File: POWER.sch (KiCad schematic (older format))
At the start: 59 parts, among them Q201 PZTA42, Q202 PZTA42, Q203 BCP51, U201 MAX1555, U202 BQ24400, U203 TPS61021A

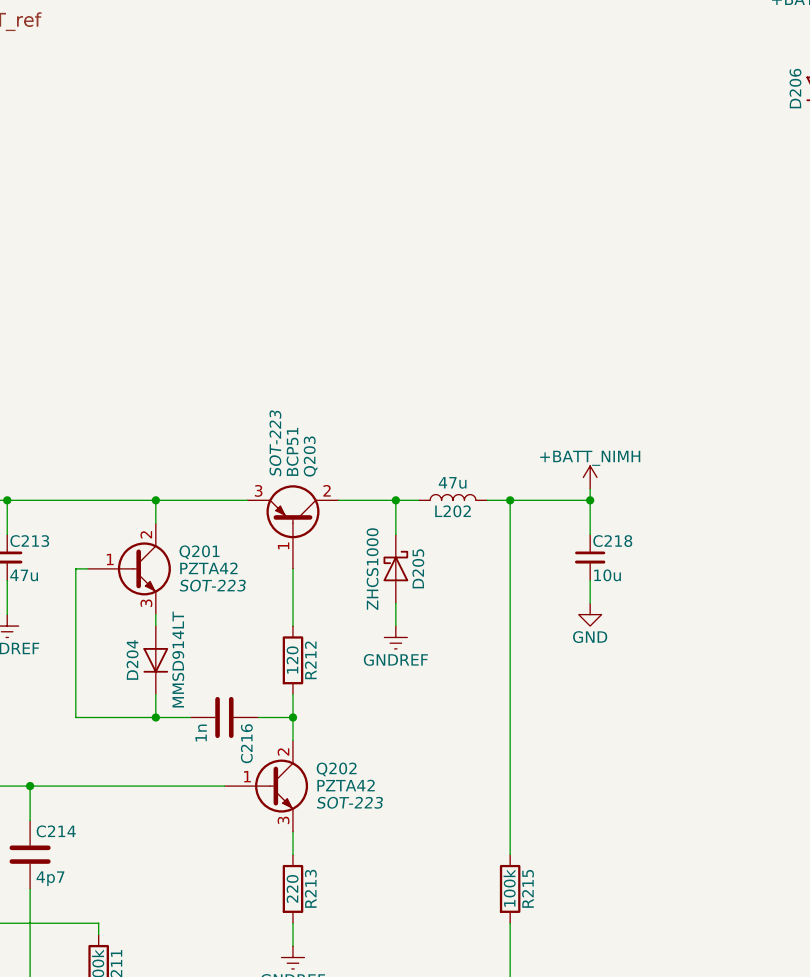
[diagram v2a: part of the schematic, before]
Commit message: Created netlist with current components Foreward Annotation to Board
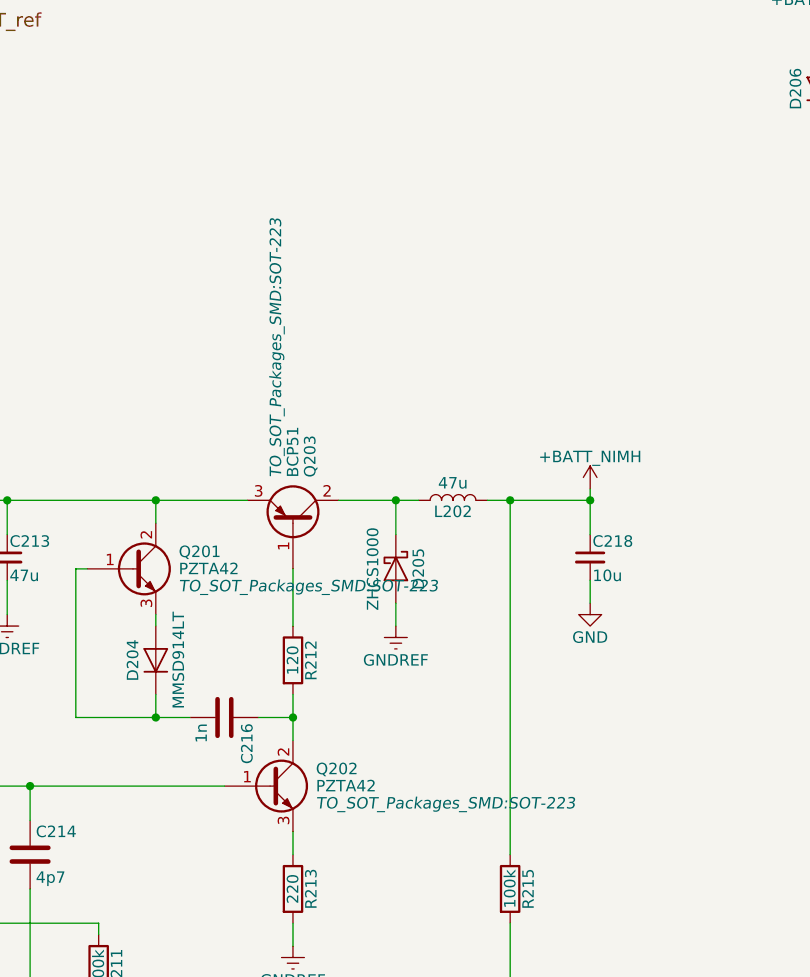
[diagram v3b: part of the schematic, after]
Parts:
- C204, C205, C206, C207, C208, C209, C210, C215, C219: footprint Capacitors_SMD:C_0603 -> Capacitors_SMD:C_0402
- C211: footprint (none) -> Capacitors_SMD:C_0603
- C212, C214, C216, C217: footprint (none) -> Capacitors_SMD:C_0402
- C213: footprint Capacitors_SMD:C_0603 -> Capacitors_SMD:C_0805
- D201, D202, D203, D204, D205, D206, D207: footprint (none) -> Diodes_SMD:DD-PAK_TO263_SingleDiode
- L201: footprint Resistors_SMD:R_0603 -> Choke_SMD:Choke_SMD_1206_Standard
- L202: footprint (none) -> Choke_SMD:Choke_SMD_1206_Standard
- Q201, Q202, Q203: footprint SOT-223 -> TO_SOT_Packages_SMD:SOT-223
- R201, R202, R203, R204, R205, R207, R208, R211, R217, R218: footprint Resistors_SMD:R_0603 -> Resistors_SMD:R_0402
- R206, R209, R210, R212, R213, R214, R215, R216: footprint (none) -> Resistors_SMD:R_0402
- TP201, TP202, TP203, TP204, TP205, TP206: footprint buttons:TP -> NokiaRetroFit:TP
- U202: footprint (none) -> SMD_Packages:SOIC-8-N

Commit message: Modification for STM32 adaption
For the Hackaday Prize 2017 I decided to switch to STM32 as CPU

*Power system was modified to just contain the charge IC,
*Boost converter for high voltage peripherals
*Buck converter for 3V3 for CPU and switchable NVCC_3V3
   for peripherie

CPU signals are routed and pinmux is done in firmware folder.

SD-Card has 4bit Interface

WiFi module ESP8266 is connected via UART

Wolfson Ausio codec is connected via SAI

Two digital microphones for noise canceling

Rumble Motor driver

LCD is connected via it's own I2C interface
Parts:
- removed C201, C218: 10u, Capacitors_SMD:C_0603, symbol C_Small
- removed C205: 100n, Capacitors_SMD:C_0402, symbol C_Small
- removed C208: 1n, Capacitors_SMD:C_0402, symbol C_Small
- removed C211: 330n, Capacitors_SMD:C_0603, symbol C
- removed C212: 2n2, Capacitors_SMD:C_0402, symbol C
- removed C213: 47u, Capacitors_SMD:C_0805, symbol C_Small
- removed C214: 4p7, Capacitors_SMD:C_0402, symbol C
- removed C216: 1n, Capacitors_SMD:C_0402, symbol C
- removed C217: 100n, Capacitors_SMD:C_0402, symbol C
- removed D201: BZT52-C5V1, Diodes_SMD:DD-PAK_TO263_SingleDiode, symbol D
- removed D202, D204, D206, D207: MMSD914LT, Diodes_SMD:DD-PAK_TO263_SingleDiode, symbol D
- removed D203: S1A, Diodes_SMD:DD-PAK_TO263_SingleDiode, symbol D
- removed D205: ZHCS1000, Diodes_SMD:DD-PAK_TO263_SingleDiode, symbol D_Schottky
- removed L202: 47u, Choke_SMD:Choke_SMD_1206_Standard, symbol L
- removed Q201, Q202: PZTA42, TO_SOT_Packages_SMD:SOT-223, symbol PZTA42
- removed Q203: BCP51, TO_SOT_Packages_SMD:SOT-223, symbol BCP51
- removed R216: 1M, Resistors_SMD:R_0402, symbol R
- removed U202: BQ24400, SMD_Packages:SOIC-8-N, symbol BQ24400
- added L202: 2u2, Choke_SMD:Choke_SMD_1206_Standard, symbol L_Small
- added U202: TPS62742, symbol TPS62742
- C204, C206, C207, C209, C210, C215, C219: footprint Capacitors_SMD:C_0402 -> Capacitors_SMD:C_0402_NoSilk
- C220: footprint Capacitors_SMD:C_0603 -> Capacitors_SMD:C_0402_NoSilk
- R201, R202, R203, R204, R207, R208, R217, R218: footprint Resistors_SMD:R_0402 -> Resistors_SMD:R_0402_NoSilk
- R205: value 1k -> 0; footprint Resistors_SMD:R_0402 -> Resistors_SMD:R_0402_NoSilk
- R206: value 6k81 -> 0; footprint Resistors_SMD:R_0402 -> Resistors_SMD:R_0402_NoSilk
- R209: value 0R05 -> 0; footprint Resistors_SMD:R_0402 -> Resistors_SMD:R_0402_NoSilk
- R210: value 1k1 -> 0; footprint Resistors_SMD:R_0402 -> Resistors_SMD:R_0402_NoSilk
- R211, R214: value 100k -> 0; footprint Resistors_SMD:R_0402 -> Resistors_SMD:R_0402_NoSilk
- R212: value 120 -> 0; footprint Resistors_SMD:R_0402 -> Resistors_SMD:R_0402_NoSilk
- R213: value 220 -> 0; footprint Resistors_SMD:R_0402 -> Resistors_SMD:R_0402_NoSilk
- R215: value 100k -> 10k; footprint Resistors_SMD:R_0402 -> Resistors_SMD:R_0402_NoSilk
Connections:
- net +BATT_LIPO: now also R205.2, R206.2, R209.2, R210.2, U202.1 (VIN), U202.12 (EN); no longer R215.1
- net GND: now also R211.1, R212.1, R213.1, R214.1, U202.13 (TP), U202.3 (GND); no longer R206.2, R209.2
- net GNDREF: no longer R209.1, R210.2, R213.2
- net ~CHARGING: no longer R211.2
- net at R210.1: now also R214.2, U202.8 (VSEL4)
- net at R206.1: now also R212.2, U202.10 (VSEL2)
- net 3V3_PG: now reaches R215.2
- net 3V3_PG: now also U202.7 (PG); no longer R214.1
- net at R205.1: now also R211.2, U202.11 (VSEL1)
- new net: L202.1, U202.2 (SW)
- new net: R209.1, R213.2, U202.9 (VSEL3)
- new net 3V3: L202.2, R215.1, U202.5 (VOUT)
- new net NVCC_3V3: U202.6 (LOAD)
- new net NVCC_3V3_EN: U202.4 (CTRL)
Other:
- note added: "LiPo min 3.7V"
- note added: "Switched Rail"
- note removed: "+15V"
- note removed: "+3.3VDAC"
- note removed: "+BATT_LIPO"
- note removed: "+BATT_NIMH"
- note removed: "-"
- note removed: "0.675V"
- note removed: "1.1V"
- note removed: "1.25A"
- note removed: "1.35V"
- note removed: "1.5A"
- note removed: "1.5V"
- note removed: "1.75A"
- note removed: "1.8V"
- note removed: "1.8V .. 3V"
- note removed: "100mA"
- note removed: "1A"
- note removed: "1V"
- note removed: "1mA"
- note removed: "2.4V"
- note removed: "2.4V NiMH option"
- note removed: "2.85V .. 3.3V"
- note removed: "2.8V"
- note removed: "250mA"
- note removed: "3,5A"
- note removed: "3.3V"
- note removed: "3.7V"
- note removed: "350mA"
- note removed: "4V"
- note removed: "4V_BST"
- note removed: "50mV max\n-50mV min"
- note removed: "5A"
- note removed: "5V"
- note removed: "5V_VBUS"
- note removed: "600mA"
- note removed: "?"
- note removed: "Battery"
- note removed: "Comment"
- note removed: "Current (max)"
- note removed: "DDR_VREF"
- note removed: "IO for A7 radio module"
- note removed: "IO for GPIO and JTAG"
- note removed: "LICELL"
- note removed: "LiPO Battery"
- note removed: "LiPo option"
- note removed: "MEM_3V3"
- note removed: "NVCC_1V8"
- note removed: "NVCC_3V3"
- note removed: "NVCC_DRAM"
- note removed: "NVCC_DRAM / 2"
- note removed: "NVCC_GPIO"
- note removed: "NVCC_SD1"
- note removed: "NVCC_SD2"
- note removed: "NVCC_SD3"
- note removed: "Net"
- note removed: "Ni-MH Battery"
- note removed: "PMIC"
- note removed: "PMIC_PWR"
- note removed: "Power domain overview"
- note removed: "Power domain tree"
- note removed: "RADIO"
- note removed: "RAM"
- note removed: "RUMBLE"
- note removed: "SW1AOUT"
- note removed: "SW1BOUT"
- note removed: "SW2OUT"
- note removed: "SW3OUT"
- note removed: "SWBSTOUT"
- note removed: "Source"
- note removed: "TPS61021A"
- note removed: "V @ BAT needs to be 2V .. 0.95V"
- note removed: "V33"
- note removed: "VDDA"
- note removed: "VDD_ARM_IN"
- note removed: "VDD_SOC_IN"
- note removed: "VDD_SPK"
- note removed: "VLDO1_1V8"
- note removed: "VLDO2_1V5"
- note removed: "VLDO3_3V3"
- note removed: "VLDO4_2V8"
- note removed: "VSNVS"
- note removed: "Voltage"
- note removed: "alternative 3.15V"
- note removed: "lt fault at 2.5V\nht fault at 1.25V\ncutoff at 1.125V\n"
- note removed: "not used"
- note removed: "one of the two batter sources"
- note removed: "small LDO for LiPo battery"
- moved on the sheet: C215, C219, C220, L201, R217, R218, TP204, TP205, TP206, U203

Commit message: Placed a lot of components and routed the audio codec
The BGA of tha audio chipset is to small for regualr technology.
We do not use all of the pins of the chip so we ignore the other
pads and escape throug the balls of the other pad.
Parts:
- U202: footprint (none) -> NokiaRetroFit:TPS6274x
- U203: footprint (none) -> Housings_SON:Texas_S-PVSON-N8_ThermalVias
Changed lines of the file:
@@
 LIBS:contrib
 LIBS:valves
-LIBS:tps62742
-LIBS:WM8994ECS
+LIBS:stm32
 LIBS:3210retro-cache
 EELAYER 26 0
@@
 F 0 "U203" H 3000 6400 60  0000 C CNN
 F 1 "TPS61021A" H 2800 6000 60  0000 C CNN
-F 2 "" H 2800 6150 60  0001 C CNN
+F 2 "Housings_SON:Texas_S-PVSON-N8_ThermalVias" H 2800 6150 60  0001 C CNN
 F 3 "" H 2800 6150 60  0000 C CNN
 	1    2800 5950
@@
 F 0 "U202" H 7700 2087 60  0000 C CNN
 F 1 "TPS62742" H 7700 1981 60  0000 C CNN
-F 2 "" H 7700 1900 60  0001 C CNN
+F 2 "NokiaRetroFit:TPS6274x" H 7700 1900 60  0001 C CNN
 F 3 "" H 7700 1900 60  0001 C CNN
 	1    7700 1500
@@
 $Bitmap
 Pos 9200 5400
-Scale 1.000000
+Scale 1,000000
 Data
 89 50 4E 47 0D 0A 1A 0A 00 00 00 0D 49 48 44 52 00 00 04 01 00 00 01 ED 08 02 00 00 00 E7 5F F0
